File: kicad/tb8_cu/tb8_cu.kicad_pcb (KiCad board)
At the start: 4 copper layers, 210 x 85 mm, 45 parts, among them J1 Conn_02x25_Counter_Clockwise, U1 74AHCT74, U10 74AHCT193, U11 74AHCT193, U12 74AHCT193, U13 74AHCT193, U14 74AHCT573, U15 74AHCT573, U16 74HC00, U17 74HC00, U18 74HCT74, U19 74AHCT573, U2 74AHCT08, U20 74AHCT573, U21 74AHCT573, U22 74AHCT573, U3 74AHCT32, U4 74AHCT573, U5 74AHCT238, U6 74AHCT238, U7 74AHCT573, U8 74AHCT00, U9 74AHCT573

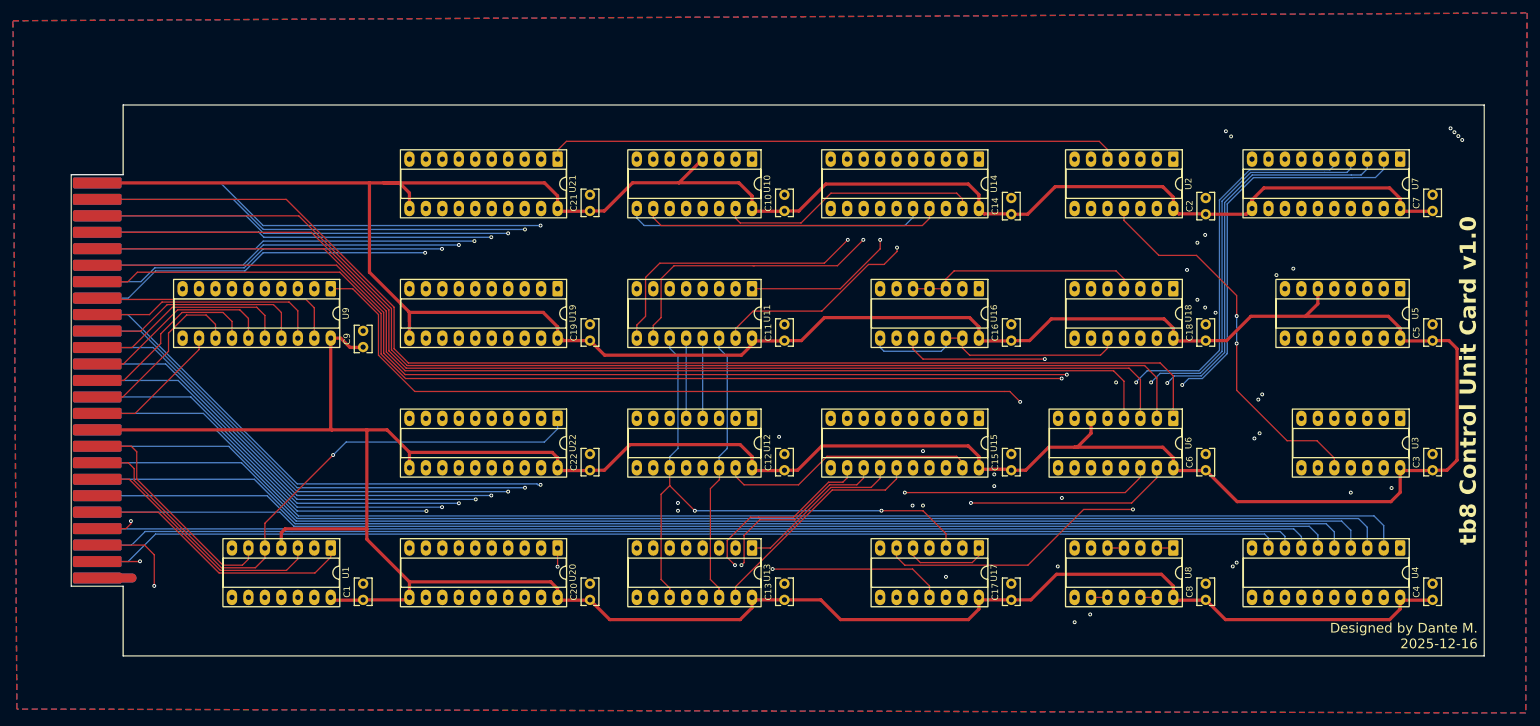
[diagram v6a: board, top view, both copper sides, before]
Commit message: fix/rotate pcb labels
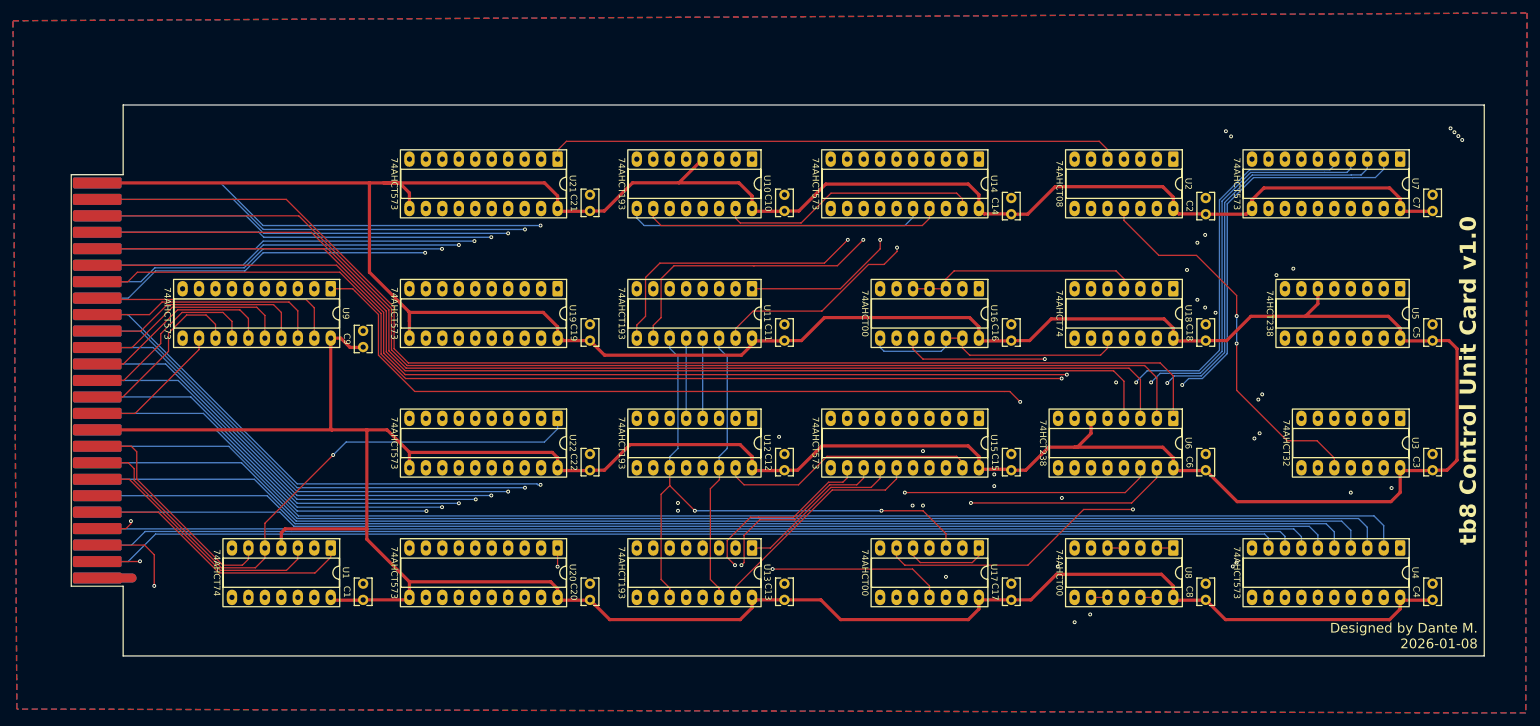
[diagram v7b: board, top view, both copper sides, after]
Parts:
- U16, U17: value 74HC00 -> 74AHCT00
- U18: value 74HCT74 -> 74AHCT74
- U5, U6: value 74AHCT238 -> 74HCT238
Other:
- board text added: "Designed by Dante M. 2026-01-08"
- board text removed: "Designed by Dante M. 2025-12-16"
